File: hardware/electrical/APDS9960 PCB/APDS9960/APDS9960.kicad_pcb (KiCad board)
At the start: 2 copper layers, 22.9 x 17.8 mm, 2 parts, among them J1 Conn_01x06, J2 Conn_01x04

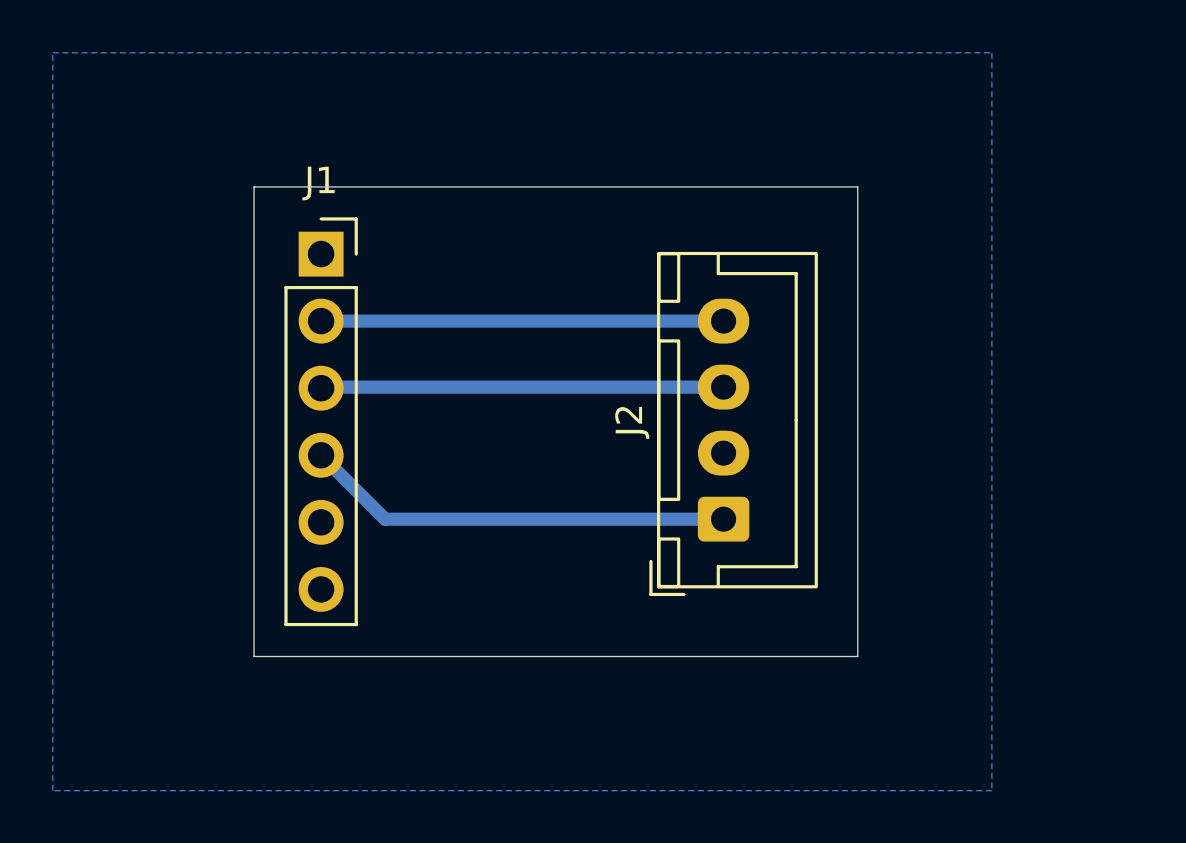
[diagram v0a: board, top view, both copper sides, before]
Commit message: backup sensor and limit switch PCBs
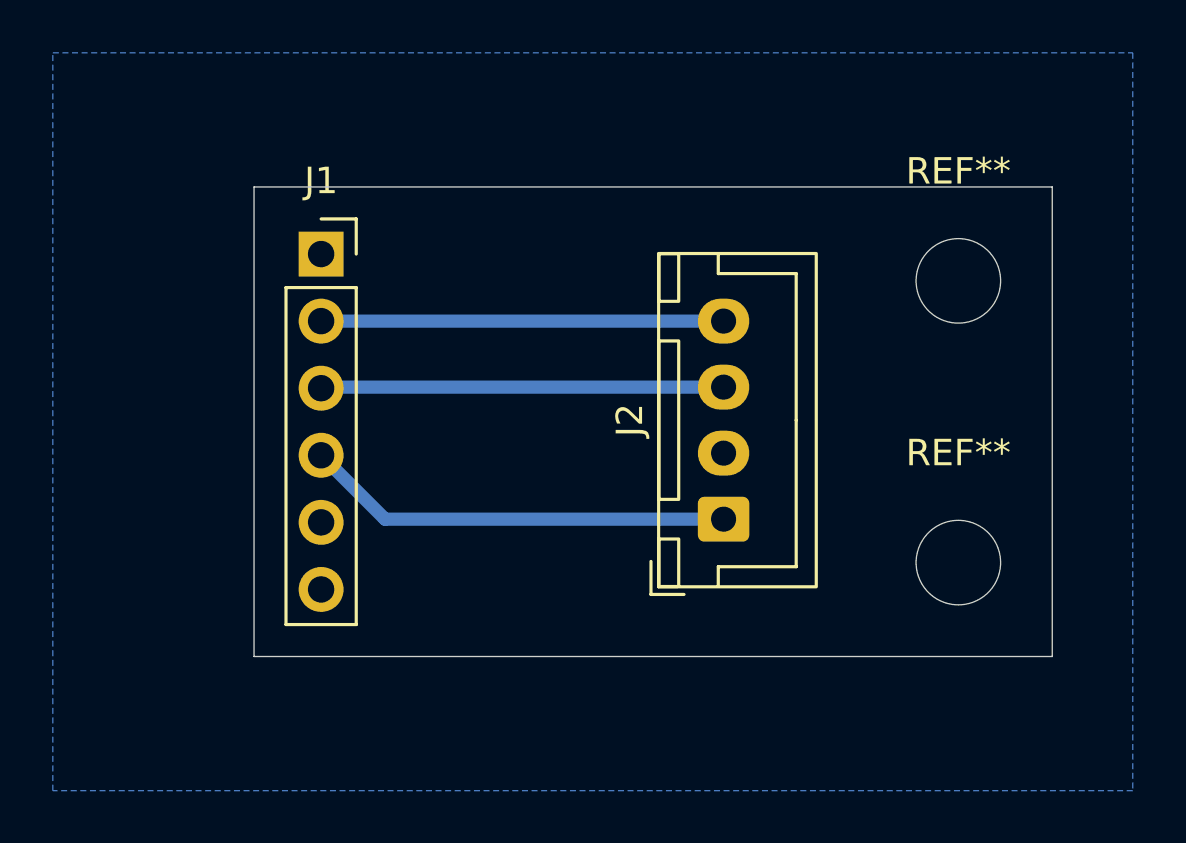
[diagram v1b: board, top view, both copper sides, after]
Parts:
- added REF**: MountingHole_3.2mm_M3, MountingHole:MountingHole_3.2mm_M3, F.Cu at (110.5, 95.5)
- added REF**: MountingHole_3.2mm_M3, MountingHole:MountingHole_3.2mm_M3, F.Cu at (110.5, 84.8)
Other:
- board size 22.9 x 17.8 mm -> 30.2 x 17.8 mm
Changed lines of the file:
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@@
 		(filling no)
 		(pcbplotparams
-			(layerselection 0x00000000_00000000_55555555_5755f5ff)
+			(layerselection 0x00000000_00000000_55555555_5755555f)
 			(plot_on_all_layers_selection 0x00000000_00000000_00000000_00000000)
 			(disableapertmacros no)
 			(usegerberextensions no)
-			(usegerberattributes yes)
-			(usegerberadvancedattributes yes)
+			(usegerberattributes no)
+			(usegerberadvancedattributes no)
 			(creategerberjobfile yes)
 			(dashed_line_dash_ratio 12)
@@
 			(outputformat 1)
 			(mirror no)
-			(drillshape 1)
+			(drillshape 0)
 			(scaleselection 1)
-			(outputdirectory "")
-		)
+			(outputdirectory "gerbers/")
+		)
+	)
+	(footprint "MountingHole:MountingHole_3.2mm_M3"
+		(layer "F.Cu")
+		(at 110.49 95.504)
+		(descr "Mounting Hole 3.2mm, M3, no annular, generated by kicad-footprint-generator mountinghole.py")
+		(tags "mountinghole M3")
+		(property "Reference" "REF**"
+			(at 0 -4.15 0)
+			(layer "F.SilkS")
+			(effects
+				(font
+					(size 1 1)
+					(thickness 0.15)
+				)
+			)
+		)
+		(property "Value" "MountingHole_3.2mm_M3"
+			(at 0 4.15 0)
+			(layer "F.Fab")
+			(effects
+				(font
+					(size 1 1)
+					(thickness 0.15)
+				)
+			)
+		)
+		(property "Datasheet" ""
+			(at 0 0 0)
+			(layer "F.Fab")
+			(hide yes)
+			(effects
+				(font
+					(size 1.27 1.27)
+				)
+			)
+		)
+		(property "Description" ""
+			(at 0 0 0)
+			(layer "F.Fab")
+			(hide yes)
+			(effects
+				(font
+					(size 1.27 1.27)
+				)
+			)
+		)
+		(property "KiLib_Generator" "mounting_hardware/mounting_hole"
+			(at 0 0 0)
+			(layer "F.SilkS")
+			(hide yes)
+			(effects
+				(font
+					(size 1 1)
+					(thickness 0.15)
+				)
+			)
+		)
+		(attr exclude_from_pos_files exclude_from_bom)
+		(duplicate_pad_numbers_are_jumpers no)
+		(fp_circle
+			(center 0 0)
+			(end 3.2 0)
+			(stroke
+				(width 0.15)
+				(type solid)
+			)
+			(fill no)
+			(layer "Cmts.User")
+		)
+		(fp_circle
+			(center 0 0)
+			(end 3.45 0)
+			(stroke
+				(width 0.05)
+				(type solid)
+			)
+			(fill no)
+			(layer "F.CrtYd")
+		)
+		(fp_text user "${REFERENCE}"
+			(at 0 0 0)
+			(layer "F.Fab")
+			(effects
+				(font
+					(size 1 1)
+					(thickness 0.15)
+				)
+			)
+		)
+		(pad "" np_thru_hole circle
+			(at 0 0)
+			(size 3.2 3.2)
+			(drill 3.2)
+			(layers "*.Cu" "*.Mask")
+		)
+		(embedded_fonts no)
+	)
+	(footprint "MountingHole:MountingHole_3.2mm_M3"
+		(layer "F.Cu")
+		(at 110.49 84.836)
+		(descr "Mounting Hole 3.2mm, M3, no annular, generated by kicad-footprint-generator mountinghole.py")
+		(tags "mountinghole M3")
+		(property "Reference" "REF**"
+			(at 0 -4.15 0)
+			(layer "F.SilkS")
+			(effects
+				(font
+					(size 1 1)
+					(thickness 0.15)
+				)
+			)
+		)
+		(property "Value" "MountingHole_3.2mm_M3"
+			(at 0 4.15 0)
+			(layer "F.Fab")
+			(effects
+				(font
+					(size 1 1)
+					(thickness 0.15)
+				)
+			)
+		)
+		(property "Datasheet" ""
+			(at 0 0 0)
+			(layer "F.Fab")
+			(hide yes)
+			(effects
+				(font
+					(size 1.27 1.27)
+				)
+			)
+		)
+		(property "Description" ""
+			(at 0 0 0)
+			(layer "F.Fab")
+			(hide yes)
+			(effects
+				(font
+					(size 1.27 1.27)
+				)
+			)
+		)
+		(property "KiLib_Generator" "mounting_hardware/mounting_hole"
+			(at 0 0 0)
+			(layer "F.SilkS")
+			(hide yes)
+			(effects
+				(font
+					(size 1 1)
+					(thickness 0.15)
+				)
+			)
+		)
+		(attr exclude_from_pos_files exclude_from_bom)
+		(duplicate_pad_numbers_are_jumpers no)
+		(fp_circle
+			(center 0 0)
+			(end 3.2 0)
+			(stroke
+				(width 0.15)
+				(type solid)
+			)
+			(fill no)
+			(layer "Cmts.User")
+		)
+		(fp_circle
+			(center 0 0)
+			(end 3.45 0)
+			(stroke
+				(width 0.05)
+				(type solid)
+			)
+			(fill no)
+			(layer "F.CrtYd")
+		)
+		(fp_text user "${REFERENCE}"
+			(at 0 0 0)
+			(layer "F.Fab")
+			(effects
+				(font
+					(size 1 1)
+					(thickness 0.15)
+				)
+			)
+		)
+		(pad "" np_thru_hole circle
+			(at 0 0)
+			(size 3.2 3.2)
+			(drill 3.2)
+			(layers "*.Cu" "*.Mask")
+		)
+		(embedded_fonts no)
 	)
 	(footprint "Connector_JST:JST_XH_B4B-XH-A_1x04_P2.50mm_Vertical"
@@
 	(gr_rect
 		(start 83.82 81.28)
-		(end 106.68 99.06)
+		(end 114.046 99.06)
 		(radius 2)
 		(stroke
@@
 		(fill no)
 		(layer "Edge.Cuts")
+	)
+	(segment
+		(start 88.78 93.86)
+		(end 86.36 91.44)
+		(width 0.5)
+		(layer "B.Cu")
+		(net "/VCC")
+	)
+	(segment
+		(start 101.6 93.86)
+		(end 88.78 93.86)
+		(width 0.5)
+		(layer "B.Cu")
+		(net "/VCC")
+	)
+	(segment
+		(start 101.6 88.86)
+		(end 86.4 88.86)
+		(width 0.5)
+		(layer "B.Cu")
+		(net "/SDA")
+	)
+	(segment
+		(start 86.4 88.86)
+		(end 86.36 88.9)
+		(width 0.5)
+		(layer "B.Cu")
+		(net "/SDA")
 	)
 	(segment
@@
 		(net "/SCL")
 	)
-	(segment
-		(start 88.78 93.86)
-		(end 86.36 91.44)
-		(width 0.5)
-		(layer "B.Cu")
-		(net "/VCC")
-	)
-	(segment
-		(start 101.6 93.86)
-		(end 88.78 93.86)
-		(width 0.5)
-		(layer "B.Cu")
-		(net "/VCC")
-	)
-	(segment
-		(start 101.6 88.86)
-		(end 86.4 88.86)
-		(width 0.5)
-		(layer "B.Cu")
-		(net "/SDA")
-	)
-	(segment
-		(start 86.4 88.86)
-		(end 86.36 88.9)
-		(width 0.5)
-		(layer "B.Cu")
-		(net "/SDA")
-	)
 	(zone
 		(net "/GND")
@@
 		(polygon
 			(pts
-				(xy 76.2 76.2) (xy 111.76 76.2) (xy 111.76 104.14) (xy 76.2 104.14)
-			)
-		)
+				(xy 76.2 76.2) (xy 117.094 76.2) (xy 117.094 104.14) (xy 76.2 104.14)
+			)
+		)
